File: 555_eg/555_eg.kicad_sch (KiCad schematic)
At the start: 41 parts, among them J1 Gate In, J2 Power Connector, J3 Envelope Out, J4 Inverted Out, Q1 2N3904, Q2 2N3904, Q3 2N3904, U1 NE555P, U2 TL074

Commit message: Start working on PCB for envelope generator
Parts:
- added C8, C9: 0.1uF, Capacitor_THT:C_Rect_L7.2mm_W2.5mm_P5.00mm_FKS2_FKP2_MKS2_MKP2, symbol Device:C_Small
- C1: renamed from C5; footprint (none) -> Capacitor_THT:C_Rect_L7.2mm_W2.5mm_P5.00mm_FKS2_FKP2_MKS2_MKP2
- C2: renamed from C6; footprint (none) -> Capacitor_THT:C_Rect_L7.2mm_W2.5mm_P5.00mm_FKS2_FKP2_MKS2_MKP2
- C3: renamed from C7; footprint (none) -> Capacitor_THT:CP_Radial_D6.3mm_P2.50mm
- C4: renamed from C1; footprint (none) -> Capacitor_THT:CP_Radial_D6.3mm_P2.50mm
- C5: renamed from C2; footprint (none) -> Capacitor_THT:CP_Radial_D6.3mm_P2.50mm
- C6: renamed from C3; footprint (none) -> Capacitor_THT:C_Rect_L7.2mm_W2.5mm_P5.00mm_FKS2_FKP2_MKS2_MKP2
- C7: renamed from C4; footprint (none) -> Capacitor_THT:C_Rect_L7.2mm_W2.5mm_P5.00mm_FKS2_FKP2_MKS2_MKP2
- J1: footprint (none) -> CustomStuff:PinHeader_1x03_P2.54mm_Vertical_AudioJack
- J2: renamed from J3; footprint (none) -> CustomStuff:PinHeader_1x03_P2.54mm_Vertical_AudioJack
- J3: renamed from J4; footprint (none) -> CustomStuff:PinHeader_1x03_P2.54mm_Vertical_AudioJack
- J4: renamed from J2; footprint (none) -> Connector_IDC:IDC-Header_2x05_P2.54mm_Vertical
- R1, R2: footprint (none) -> Resistor_THT:R_Axial_DIN0207_L6.3mm_D2.5mm_P10.16mm_Horizontal
- R10: renamed from R11; footprint (none) -> Resistor_THT:R_Axial_DIN0207_L6.3mm_D2.5mm_P10.16mm_Horizontal
- R11: renamed from R13; footprint (none) -> Resistor_THT:R_Axial_DIN0207_L6.3mm_D2.5mm_P10.16mm_Horizontal
- R12: renamed from R14; footprint (none) -> Resistor_THT:R_Axial_DIN0207_L6.3mm_D2.5mm_P10.16mm_Horizontal
- R13: renamed from R3; footprint (none) -> Resistor_THT:R_Axial_DIN0207_L6.3mm_D2.5mm_P10.16mm_Horizontal
- R14: renamed from R4; footprint (none) -> Resistor_THT:R_Axial_DIN0207_L6.3mm_D2.5mm_P10.16mm_Horizontal
- R3: renamed from R5; footprint (none) -> Resistor_THT:R_Axial_DIN0207_L6.3mm_D2.5mm_P10.16mm_Horizontal
- R4: renamed from R6; footprint (none) -> Resistor_THT:R_Axial_DIN0207_L6.3mm_D2.5mm_P10.16mm_Horizontal
- R5: renamed from R7; footprint (none) -> Resistor_THT:R_Axial_DIN0207_L6.3mm_D2.5mm_P10.16mm_Horizontal
- R6: renamed from R8; footprint (none) -> Resistor_THT:R_Axial_DIN0207_L6.3mm_D2.5mm_P10.16mm_Horizontal
- R7: renamed from R10; footprint (none) -> Resistor_THT:R_Axial_DIN0207_L6.3mm_D2.5mm_P10.16mm_Horizontal
- R8: renamed from R9; footprint (none) -> Resistor_THT:R_Axial_DIN0207_L6.3mm_D2.5mm_P10.16mm_Horizontal
- R9: renamed from R12; footprint (none) -> Resistor_THT:R_Axial_DIN0207_L6.3mm_D2.5mm_P10.16mm_Horizontal
- RV1, RV2: footprint (none) -> Connector_PinHeader_2.54mm:PinHeader_1x03_P2.54mm_Vertical
- RV3: renamed from RV4; footprint (none) -> Connector_PinHeader_2.54mm:PinHeader_1x03_P2.54mm_Vertical
- RV4: renamed from RV3; footprint (none) -> Connector_PinHeader_2.54mm:PinHeader_1x03_P2.54mm_Vertical
- U2: footprint (none) -> Package_DIP:DIP-14_W7.62mm_Socket
- renumbered D4 to D2, D5 to D3, D6 to D4, D7 to D5, D2 to D6, D3 to D7
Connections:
- net +12V: now also U2.4 (V+), C8.1
- net -12V: now also U2.11 (V-), C9.2
- net GND: now also U2.12 (+), C8.2, C9.1
- net at U2.13 (-): now also U2.14
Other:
- moved on the sheet: U2D, U2E

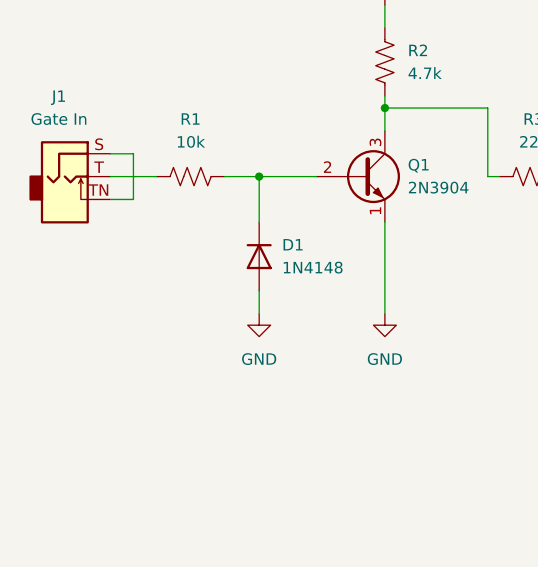
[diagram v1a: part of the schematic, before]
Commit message: Finish eg pcb, almost done panel
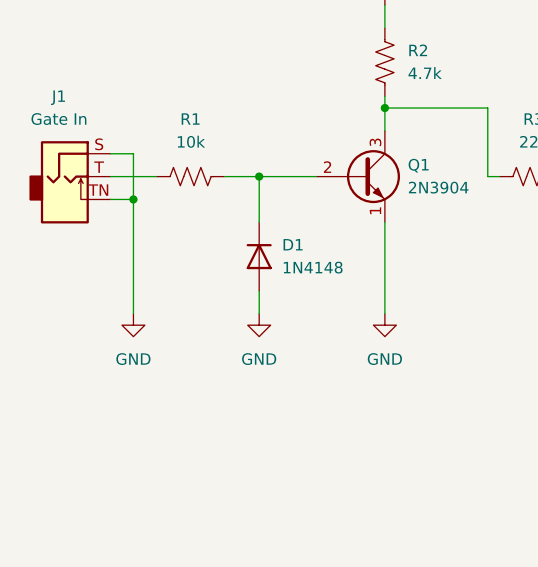
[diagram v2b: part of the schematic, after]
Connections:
- net GND: now also J1.S, J1.TN
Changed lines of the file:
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@@
+	)
+	(junction
+		(at 26.67 93.98)
+		(diameter 0)
+		(color 0 0 0 0)
 	)
 	(junction
@@
 		(pts
 			(xy 156.21 93.98) (xy 146.05 93.98)
+		)
+		(stroke
+			(width 0)
+			(type default)
+		)
+	)
+	(wire
+		(pts
+			(xy 26.67 93.98) (xy 26.67 106.68)
 		)
 		(stroke
@@
 					(unit 1)
 				)
+			)
+		)
+	)
+	(symbol
+		(lib_id "power:GND")
+		(at 26.67 106.68 0)
+		(mirror y)
+		(unit 1)
+		(exclude_from_sim no)
+		(in_bom yes)
+		(on_board yes)
+		(dnp no)
+		(property "Reference" "#PWR01"
+			(at 26.67 113.03 0)
+			(effects
+				(font
+					(size 1.27 1.27)
+				)
+				(hide yes)
+			)
+		)
+		(property "Value" "GND"
+			(at 26.67 111.76 0)
+			(effects
+				(font
+					(size 1.27 1.27)
+				)
+			)
+		)
+		(property "Footprint" ""
+			(at 26.67 106.68 0)
+			(effects
+				(font
+					(size 1.27 1.27)
+				)
+				(hide yes)
+			)
+		)
+		(property "Datasheet" ""
+			(at 26.67 106.68 0)
+			(effects
+				(font
+					(size 1.27 1.27)
+				)
+				(hide yes)
+			)
+		)
+		(property "Description" "Power symbol creates a global label with name \"GND\" , ground"
+			(at 26.67 106.68 0)
+			(effects
+				(font
+					(size 1.27 1.27)
+				)
+				(hide yes)
+			)
+		)
+		(pin "1"
+		)
+		(instances
+			(project "555_eg"
+				(path "/5fafaa57-41f0-4c5c-90c4-7760594d41fd"
+					(reference "#PWR01")
+					(unit 1)
+				)
